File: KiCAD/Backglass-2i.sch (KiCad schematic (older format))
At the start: 52 parts, among them J1 IO Header, J11 Header_ICSP_AVR, J12 Header_ICSP_AVR, J13 Header_ICSP_AVR, J2 RAMP Header, J3 LOSE Header, J4 Micro_USB_Connector, J5 Batteries, Q1 MOSFET_N_E_Dual, Q2 MOSFET_N_E_Dual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

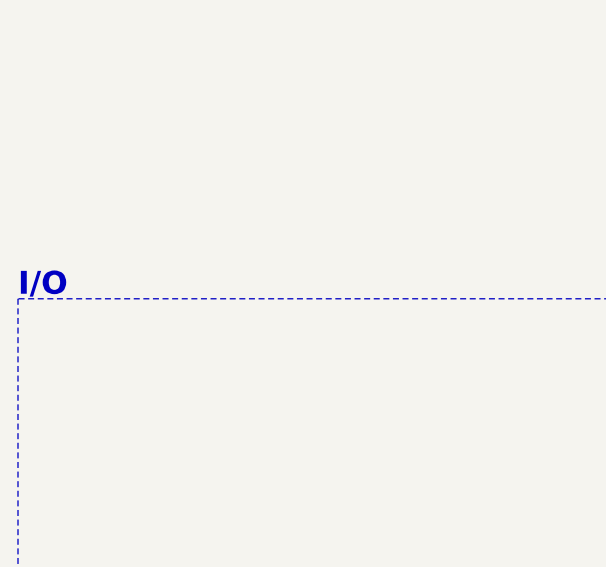
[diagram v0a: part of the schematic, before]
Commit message: Minor versioning updates
Changed Git.io link on silkscreen, updated version of schematic to 2.1, made note of changing I/O section.
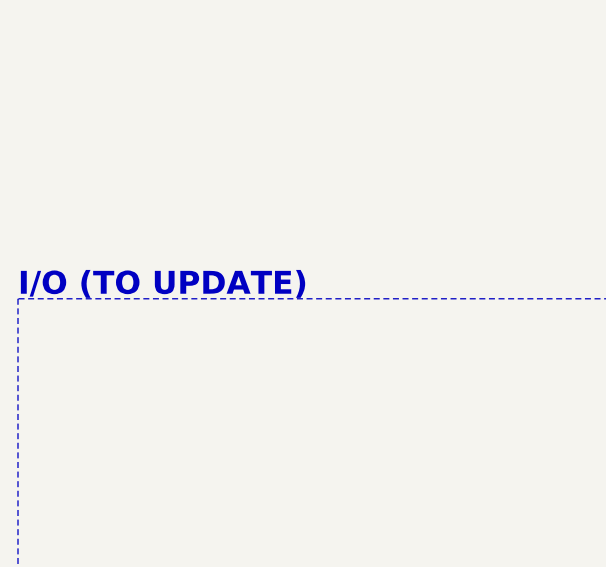
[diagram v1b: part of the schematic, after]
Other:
- note added: "I/O (TO UPDATE)"
- note removed: "I/O"
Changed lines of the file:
@@
 Title "\"Backglass 2\" Pinball Controller"
 Date "2019-05-22"
-Rev "2.0"
+Rev "2.1"
 Comp "Ana Tavares"
 Comment1 ""
@@
 $EndComp
 Text Notes 600  8200 0    100  ~ 20
-I/O
+I/O (TO UPDATE)
 Text Notes 5700 8200 0    100  ~ 20
 Output Drivers

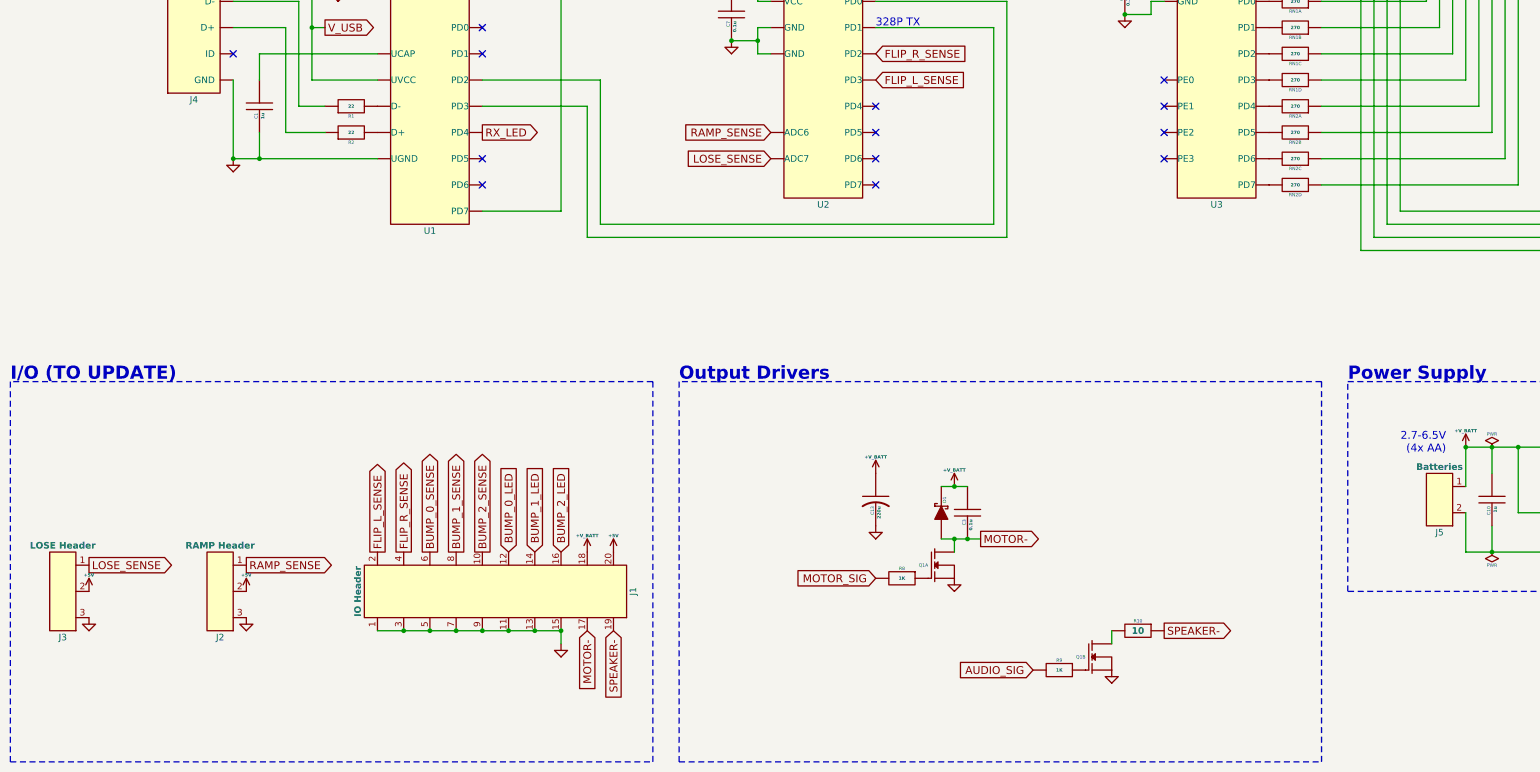
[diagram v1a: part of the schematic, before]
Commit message: Updated layout
Changed I/O connector and rerouted traces, removed I/O labels, updated logo
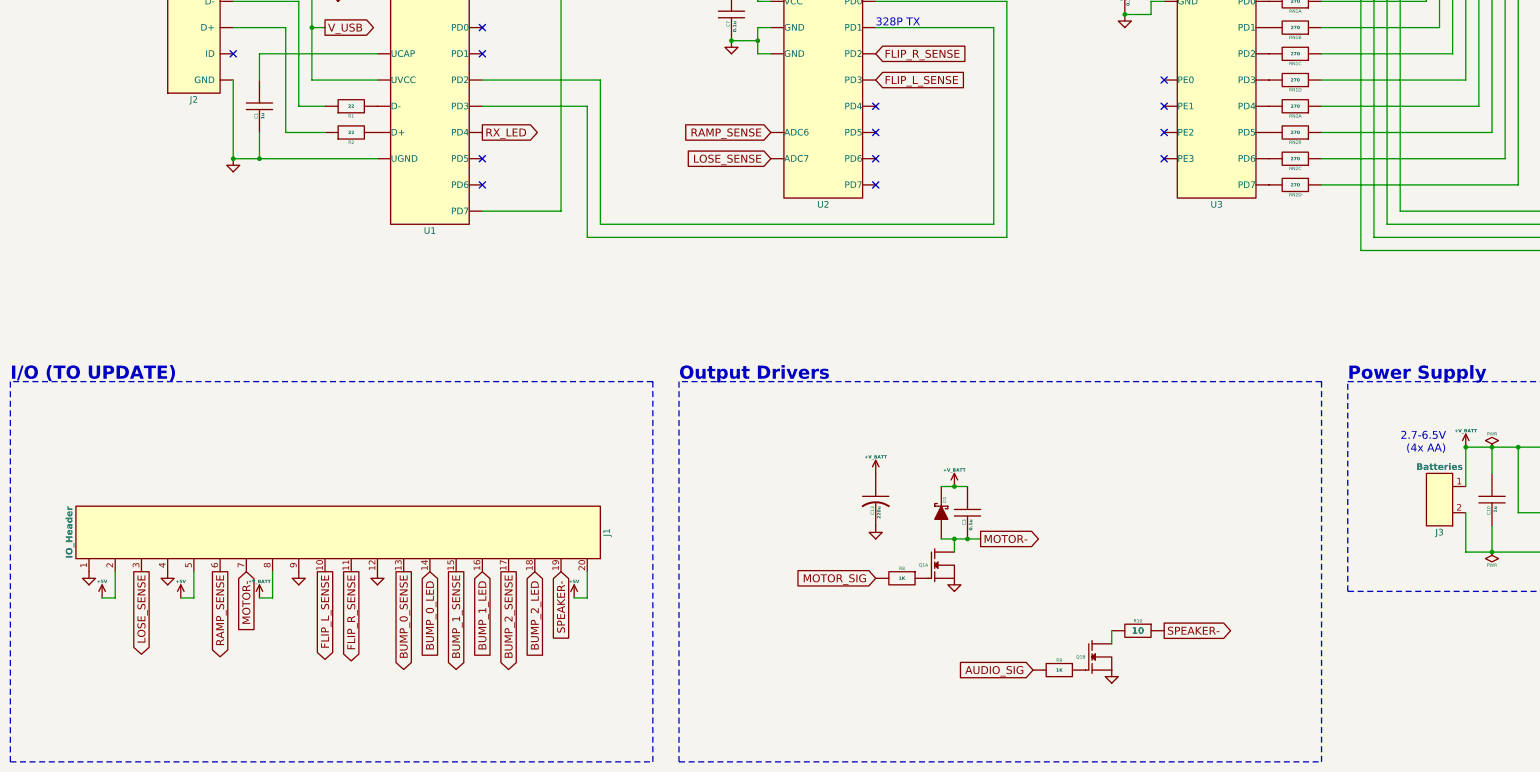
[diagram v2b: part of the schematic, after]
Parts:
- removed J1: IO Header, I_Through-hole:10x2_0.1in, symbol Header_10x2
- removed J2: RAMP Header, I_Through-hole:3x1_0.1in, symbol HEADER_3x1
- removed J3: LOSE Header, I_Through-hole:3x1_0.1in, symbol HEADER_3x1
- added J1: IO_Header, X_Proprietary:TE_1-746610-5, symbol Header_20x1_DWTB
- renumbered J4 to J2, J5 to J3
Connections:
- net +5V: now also J1.2, J1.20, J1.5
- net +V_BATT: now also J1.8
- net BUMP_0_LED: now also J1.14
- net BUMP_0_SENSE: now also J1.13
- net BUMP_1_LED: now also J1.16
- net BUMP_1_SENSE: now also J1.15
- net BUMP_2_LED: now also J1.18
- net BUMP_2_SENSE: now also J1.17
- net FLIP_L_SENSE: now also J1.10
- net FLIP_R_SENSE: now also J1.11
- net GND: now also J1.1, J1.12, J1.4, J1.9
- net LOSE_SENSE: now also J1.3
- net MOTOR-: now also J1.7
- net RAMP_SENSE: now also J1.6
- net SPEAKER-: now also J1.19
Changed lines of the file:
@@
 EESchema Schematic File Version 2
+LIBS:arduino
+LIBS:audio
+LIBS:barrel
+LIBS:bbd
+LIBS:comparator
+LIBS:data
+LIBS:diode
+LIBS:driver
+LIBS:electromechanical
+LIBS:logic
+LIBS:microcontroller
+LIBS:opamp
+LIBS:passive
+LIBS:power
+LIBS:sensor
+LIBS:switch
+LIBS:transistor
 LIBS:Backglass-2i-cache
 EELAYER 25 0
@@
 Sheet 1 1
 Title "\"Backglass 2\" Pinball Controller"
-Date "2019-05-22"
+Date "2019-06-12"
 Rev "2.1"
 Comp "Ana Tavares"
@@
 MOTOR-
 $Comp
-L Micro_USB_Connector J4
+L Micro_USB_Connector J2
 U 1 1 58E6D55C
 P 2200 6000
-F 0 "J4" H 2000 5950 50  0000 C CNN
+F 0 "J2" H 2000 5950 50  0000 C CNN
 F 1 "Micro_USB_Connector" H 2000 7050 50  0000 C CNB
 F 2 "X_Proprietary:Molex_1051640001" H 2600 6600 60  0001 C CNN
@@
 $EndComp
 $Comp
-L HEADER_2x1 J5
+L HEADER_2x1 J3
 U 1 1 58EC6D6E
 P 11600 9300
-F 0 "J5" H 11700 9250 50  0000 C CNN
+F 0 "J3" H 11700 9250 50  0000 C CNN
 F 1 "Batteries" H 11700 9750 50  0000 C CNB
 F 2 "I_Through-hole:2x1_0.1in" H 12000 9900 60  0001 C CNN
@@
 	0    -1   -1   0
 $EndComp
-$Comp
-L HEADER_3x1 J3
-U 1 1 58EEF0DA
-P 1100 10100
-F 0 "J3" H 1200 10050 50  0000 C CNN
-F 1 "LOSE Header" H 1200 10750 50  0000 C CNB
-F 2 "I_Through-hole:3x1_0.1in" H 1500 10700 60  0001 C CNN
-F 3 "" H 1500 10700 60  0001 C CNN
-	1    1100 10100
-	-1   0    0    -1
-$EndComp
-$Comp
-L HEADER_3x1 J2
-U 1 1 58EEF1DF
-P 2300 10100
-F 0 "J2" H 2400 10050 50  0000 C CNN
-F 1 "RAMP Header" H 2400 10750 50  0000 C CNB
-F 2 "I_Through-hole:3x1_0.1in" H 2700 10700 60  0001 C CNN
-F 3 "" H 2700 10700 60  0001 C CNN
-	1    2300 10100
-	-1   0    0    -1
-$EndComp
-$Comp
-L Header_10x2 J1
-U 1 1 58EF4E08
-P 5300 10000
-F 0 "J1" H 5500 9950 50  0000 C CNN
-F 1 "IO Header" H 5500 12050 50  0000 C CNB
-F 2 "I_Through-hole:10x2_0.1in" H 5700 11000 60  0001 C CNN
-F 3 "" H 5700 11000 60  0001 C CNN
-	1    5300 10000
-	0    -1   -1   0
-$EndComp
-Text GLabel 3400 9500 1    60   Output ~ 0
+Text GLabel 3000 9650 3    60   Output ~ 0
 FLIP_L_SENSE
-Text GLabel 3600 9500 1    60   Output ~ 0
+Text GLabel 3200 9650 3    60   Output ~ 0
 FLIP_R_SENSE
-Text GLabel 3800 9500 1    60   Output ~ 0
+Text GLabel 3600 9650 3    60   Output ~ 0
 BUMP_0_SENSE
-Text GLabel 4000 9500 1    60   Output ~ 0
+Text GLabel 4000 9650 3    60   Output ~ 0
 BUMP_1_SENSE
-Text GLabel 4200 9500 1    60   Output ~ 0
+Text GLabel 4400 9650 3    60   Output ~ 0
 BUMP_2_SENSE
-Text GLabel 4400 9500 1    60   Input ~ 0
+Text GLabel 3800 9650 3    60   Input ~ 0
 BUMP_0_LED
-Text GLabel 4600 9500 1    60   Input ~ 0
+Text GLabel 4200 9650 3    60   Input ~ 0
 BUMP_1_LED
-Text GLabel 4800 9500 1    60   Input ~ 0
+Text GLabel 4600 9650 3    60   Input ~ 0
 BUMP_2_LED
-Text GLabel 5200 10100 3    60   Input ~ 0
+Text GLabel 4800 9650 3    60   Input ~ 0
 SPEAKER-
-Text GLabel 5000 10100 3    60   Input ~ 0
+Text GLabel 2400 9650 3    60   Input ~ 0
 MOTOR-
+Text GLabel 1600 9650 3    60   Output ~ 0
+LOSE_SENSE
+Text GLabel 2200 9650 3    60   Output ~ 0
+RAMP_SENSE
 $Comp
 L GND #PWR034
-U 1 1 58EFDA4C
-P 4800 10200
-F 0 "#PWR034" H 4800 10025 25  0001 C CNN
-F 1 "GND" H 4800 10075 25  0001 C CNB
-F 2 "" H 4800 10200 50  0000 C CNN
-F 3 "" H 4800 10200 50  0000 C CNN
-	1    4800 10200
-	1    0    0    -1
-$EndComp
-Text GLabel 1200 9600 2    60   Output ~ 0
-LOSE_SENSE
-Text GLabel 2400 9600 2    60   Output ~ 0
-RAMP_SENSE
+U 1 1 58EFF71B
+P 1800 9650
+F 0 "#PWR034" H 1800 9475 25  0001 C CNN
+F 1 "GND" H 1800 9525 25  0001 C CNB
+F 2 "" H 1800 9650 50  0000 C CNN
+F 3 "" H 1800 9650 50  0000 C CNN
+	1    1800 9650
+	1    0    0    -1
+$EndComp
 $Comp
 L GND #PWR035
-U 1 1 58EFF71B
-P 2400 10000
-F 0 "#PWR035" H 2400 9825 25  0001 C CNN
-F 1 "GND" H 2400 9875 25  0001 C CNB
-F 2 "" H 2400 10000 50  0000 C CNN
-F 3 "" H 2400 10000 50  0000 C CNN
-	1    2400 10000
-	1    0    0    -1
-$EndComp
-$Comp
-L GND #PWR036
 U 1 1 58EFF7EF
-P 1200 10000
-F 0 "#PWR036" H 1200 9825 25  0001 C CNN
-F 1 "GND" H 1200 9875 25  0001 C CNB
-F 2 "" H 1200 10000 50  0000 C CNN
-F 3 "" H 1200 10000 50  0000 C CNN
-	1    1200 10000
+P 1200 9650
+F 0 "#PWR035" H 1200 9475 25  0001 C CNN
+F 1 "GND" H 1200 9525 25  0001 C CNB
+F 2 "" H 1200 9650 50  0000 C CNN
+F 3 "" H 1200 9650 50  0000 C CNN
+	1    1200 9650
+	1    0    0    -1
+$EndComp
+$Comp
+L +5V #PWR036
+U 1 1 58EFF8C3
+P 1300 9850
+F 0 "#PWR036" H 1300 10025 25  0001 C CNN
+F 1 "+5V" H 1300 9975 25  0000 C CNB
+F 2 "" H 1300 9850 50  0000 C CNN
+F 3 "" H 1300 9850 50  0000 C CNN
+	1    1300 9850
 	1    0    0    -1
 $EndComp
 $Comp
 L +5V #PWR037
-U 1 1 58EFF8C3
-P 1200 9800
-F 0 "#PWR037" H 1200 9975 25  0001 C CNN
-F 1 "+5V" H 1200 9925 25  0000 C CNB
-F 2 "" H 1200 9800 50  0000 C CNN
-F 3 "" H 1200 9800 50  0000 C CNN
-	1    1200 9800
-	1    0    0    -1
-$EndComp
-$Comp
-L +5V #PWR038
 U 1 1 58EFF997
-P 2400 9800
-F 0 "#PWR038" H 2400 9975 25  0001 C CNN
-F 1 "+5V" H 2400 9925 25  0000 C CNB
-F 2 "" H 2400 9800 50  0000 C CNN
-F 3 "" H 2400 9800 50  0000 C CNN
-	1    2400 9800
+P 1900 9850
+F 0 "#PWR037" H 1900 10025 25  0001 C CNN
+F 1 "+5V" H 1900 9975 25  0000 C CNB
+F 2 "" H 1900 9850 50  0000 C CNN
+F 3 "" H 1900 9850 50  0000 C CNN
+	1    1900 9850
 	1    0    0    -1
 $EndComp
@@
 Power Supply
 $Comp
-L +V_BATT #PWR039
+L +V_BATT #PWR038
 U 1 1 58F0AE2A
 P 7200 8900
-F 0 "#PWR039" H 7200 9075 25  0001 C CNN
+F 0 "#PWR038" H 7200 9075 25  0001 C CNN
 F 1 "+V_BATT" H 7200 9025 25  0000 C CNB
 F 2 "" H 7200 8900 50  0000 C CNN
@@
 $EndComp
 $Comp
-L GND #PWR040
+L GND #PWR039
 U 1 1 58F231B6
 P 13600 5100
-F 0 "#PWR040" H 13600 4925 25  0001 C CNN
+F 0 "#PWR039" H 13600 4925 25  0001 C CNN
 F 1 "GND" H 13600 4975 25  0001 C CNB
 F 2 "" H 13600 5100 50  0000 C CNN
@@
 NoConn ~ 7200 6500
 $Comp
-L GND #PWR041
+L GND #PWR040
 U 1 1 58F30445
 P 5600 2900
-F 0 "#PWR041" H 5600 2725 25  0001 C CNN
+F 0 "#PWR040" H 5600 2725 25  0001 C CNN
 F 1 "GND" H 5600 2775 25  0001 C CNB
 F 2 "" H 5600 2900 50  0000 C CNN
@@
 $EndComp
 $Comp
-L PWR #FLG042
+L PWR #FLG041
 U 1 1 58F90CB2
 P 11900 8700
-F 0 "#FLG042" H 11900 8795 50  0001 C CNN
+F 0 "#FLG041" H 11900 8795 50  0001 C CNN
 F 1 "PWR" H 11900 8800 25  0000 C CNN
 F 2 "" H 11900 8700 50  0000 C CNN
@@
 $EndComp
 $Comp
-L PWR #FLG043
+L PWR #FLG042
 U 1 1 58F913FE
 P 13700 8700
-F 0 "#FLG043" H 13700 8795 50  0001 C CNN
+F 0 "#FLG042" H 13700 8795 50  0001 C CNN
 F 1 "PWR" H 13700 8800 25  0000 C CNN
 F 2 "" H 13700 8700 50  0000 C CNN
@@
 $EndComp
 $Comp
-L PWR #FLG044
+L PWR #FLG043
 U 1 1 58F98F22
 P 11900 9500
-F 0 "#FLG044" H 11900 9595 50  0001 C CNN
+F 0 "#FLG043" H 11900 9595 50  0001 C CNN
 F 1 "PWR" H 11900 9600 25  0000 C CNN
 F 2 "" H 11900 9500 50  0000 C CNN
@@
 $EndComp
 $Comp
-L +V_BATT #PWR045
+L +V_BATT #PWR044
 U 1 1 58FAC448
-P 5000 9500
-F 0 "#PWR045" H 5000 9675 25  0001 C CNN
-F 1 "+V_BATT" H 5000 9625 25  0000 C CNB
-F 2 "" H 5000 9500 50  0000 C CNN
-F 3 "" H 5000 9500 50  0000 C CNN
-	1    5000 9500
-	1    0    0    -1
-$EndComp
-$Comp
-L PWR #FLG046
+P 2500 9850
+F 0 "#PWR044" H 2500 10025 25  0001 C CNN
+F 1 "+V_BATT" H 2500 9975 25  0000 C CNB
+F 2 "" H 2500 9850 50  0000 C CNN
+F 3 "" H 2500 9850 50  0000 C CNN
+	1    2500 9850
+	1    0    0    -1
+$EndComp
+$Comp
+L PWR #FLG045
 U 1 1 58F914D8
 P 14900 8700
-F 0 "#FLG046" H 14900 8795 50  0001 C CNN
+F 0 "#FLG045" H 14900 8795 50  0001 C CNN
 F 1 "PWR" H 14900 8800 25  0000 C CNN
 F 2 "" H 14900 8700 50  0000 C CNN
@@
 	12300 3900 12100 3900
 Connection ~ 11700 8700
-Wire Wire Line
-	3400 10100 4800 10100
-Connection ~ 4600 10100
-Connection ~ 4400 10100
-Connection ~ 4200 10100
-Connection ~ 4000 10100
-Connection ~ 3800 10100
-Connection ~ 3600 10100
-Wire Wire Line
-	4800 10100 4800 10200
-Connection ~ 4800 10100
 Wire Notes Line
 	15900 9800 10800 9800
@@
 	14500 8900 14500 8700
 $Comp
-L +5V #PWR047
+L +5V #PWR046
 U 1 1 58FDEEAA
-P 5200 9500
-F 0 "#PWR047" H 5200 9675 25  0001 C CNN
-F 1 "+5V" H 5200 9625 25  0000 C CNB
-F 2 "" H 5200 9500 50  0000 C CNN
-F 3 "" H 5200 9500 50  0000 C CNN
-	1    5200 9500
+P 4900 9850
+F 0 "#PWR046" H 4900 10025 25  0001 C CNN
+F 1 "+5V" H 4900 9975 25  0000 C CNB
+F 2 "" H 4900 9850 50  0000 C CNN
+F 3 "" H 4900 9850 50  0000 C CNN
+	1    4900 9850
 	1    0    0    -1
 $EndComp
@@
 	-1   0    0    1
 $EndComp
+$Comp
+L GND #PWR047
+U 1 1 5CE63F2E
+P 2800 9650
+F 0 "#PWR047" H 2800 9475 25  0001 C CNN
+F 1 "GND" H 2800 9525 25  0001 C CNB
+F 2 "" H 2800 9650 50  0000 C CNN
+F 3 "" H 2800 9650 50  0000 C CNN
+	1    2800 9650
+	1    0    0    -1
+$EndComp
+$Comp
+L GND #PWR048
+U 1 1 5CE63FC2
+P 3400 9650
+F 0 "#PWR048" H 3400 9475 25  0001 C CNN
+F 1 "GND" H 3400 9525 25  0001 C CNB
+F 2 "" H 3400 9650 50  0000 C CNN
+F 3 "" H 3400 9650 50  0000 C CNN
+	1    3400 9650
+	1    0    0    -1
+$EndComp
+Wire Wire Line
+	1300 9850 1400 9850
+Wire Wire Line
+	1400 9850 1400 9650
+Wire Wire Line
+	1900 9850 2000 9850
+Wire Wire Line
+	2000 9850 2000 9650
+Wire Wire Line
+	2500 9850 2600 9850
+Wire Wire Line
+	2600 9850 2600 9650
+Wire Wire Line
+	4900 9850 5000 9850
+Wire Wire Line
+	5000 9850 5000 9650
+$Comp
+L Header_20x1_DWTB J1
+U 1 1 5CE6F9AE
+P 5100 9550
+F 0 "J1" H 5300 9500 50  0000 C CNN
+F 1 "IO_Header" H 5300 13600 50  0000 C CNB
+F 2 "X_Proprietary:TE_1-746610-5" H 5500 10550 60  0001 C CNN
+F 3 "" H 5500 10550 60  0001 C CNN
+	1    5100 9550
+	0    -1   -1   0
+$EndComp
 $EndSCHEMATC
